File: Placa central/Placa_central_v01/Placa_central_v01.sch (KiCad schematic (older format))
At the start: 34 parts, among them J1 Conn_8.4V_PlacaAlimentação, J16 Conn_01x01_Motor1PonteHPCB, J2 Conn_01x02_ArduinoTxRx, J26 Conn_02x08_Odd_Even, J27 Conn_01x01_Motor2PonteHPCB, J28 Conn_01x01_Motor1PCBMotor, J29 Conn_01x01_Motor2PCBMotor, J3 Conn_01x01_ArduinoReset, J37 Conn_01x01_8.4VPonteH, J38 Conn_01x01_5VPonteH, J39 Conn_01x01_GNDPonteH, J4 Conn_GND_PlacaAlimentação, J40 Conn_01x01_Motor1PWM, J41 Conn_01x01_Motor1Dir1, J42 Conn_01x01_Motor1Dir2, J43 Conn_01x01_Motor2Dir1, J44 Conn_01x01_Motor2Dir2, J45 Conn_01x01_Motor2PWM, J48 Conn_01x01_5VEncoderEsq, J49 Conn_01x01_OutputEncoderEsq, J50 Conn_01x01_GNDEncoderEsq, J51 Conn_01x01_5VEncoderDir, J52 Conn_01x01_OutputEncoderDir, J53 Conn_01x01_GNDEncoderDir, SW3 SW_comando1

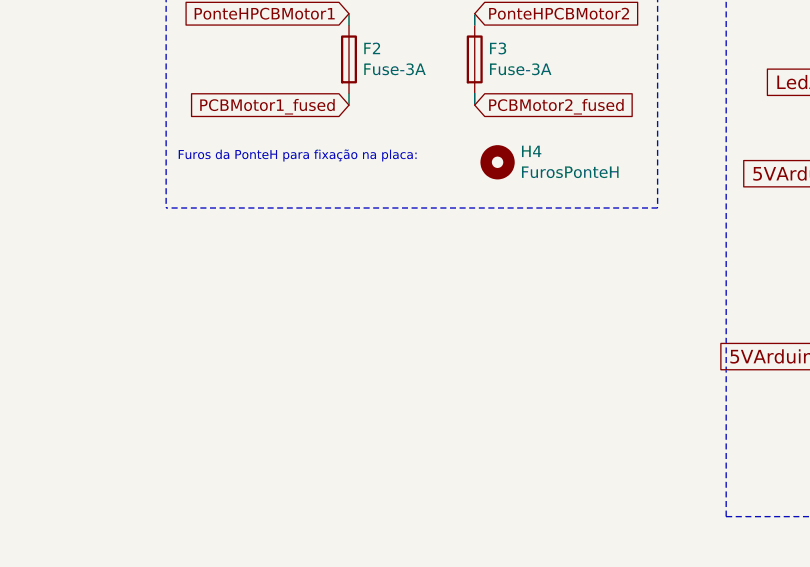
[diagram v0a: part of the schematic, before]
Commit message: Adicionada a zona de malha de ground, furos pendentes.
A zona de ground ainda não foi preenchida pois os furos da placa para fixação no acrílico requerem atualização.
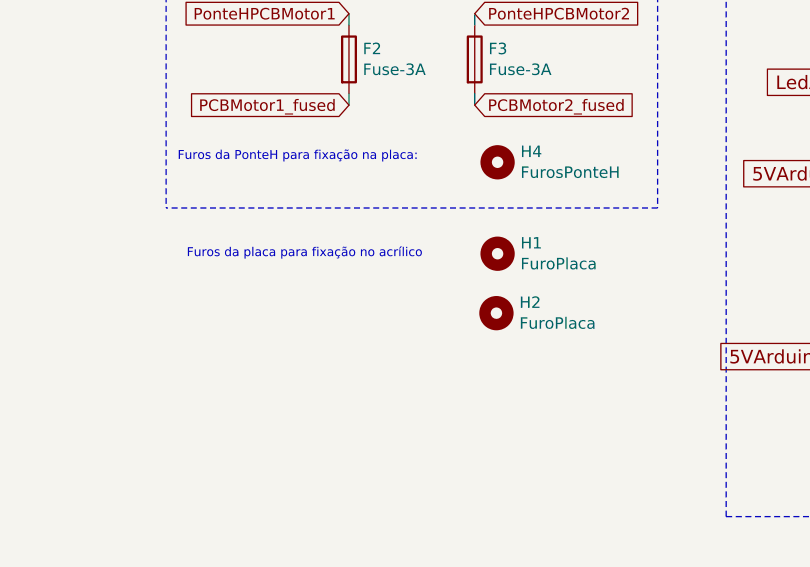
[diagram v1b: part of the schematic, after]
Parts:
- added H1, H2: FuroPlaca, Connector_Wire:SolderWirePad_1x01_Drill1mm, symbol Mechanical:MountingHole
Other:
- note added: "Furos da placa para fixação no acrílico"
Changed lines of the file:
@@
 Text GLabel 1650 2950 0    50   Input ~ 0
 ArduinoD13
+$Comp
+L Mechanical:MountingHole H1
+U 1 1 5D4C0D66
+P 7700 4050
+F 0 "H1" H 7800 4096 50  0000 L CNN
+F 1 "FuroPlaca" H 7800 4005 50  0000 L CNN
+F 2 "Connector_Wire:SolderWirePad_1x01_Drill1mm" H 7700 4050 50  0001 C CNN
+F 3 "~" H 7700 4050 50  0001 C CNN
+	1    7700 4050
+	1    0    0    -1
+$EndComp
+Text Notes 6340 4075 0    39   ~ 0
+Furos da placa para fixação no acrílico
+$Comp
+L Mechanical:MountingHole H2
+U 1 1 5D4C717E
+P 7695 4310
+F 0 "H2" H 7795 4356 50  0000 L CNN
+F 1 "FuroPlaca" H 7795 4265 50  0000 L CNN
+F 2 "Connector_Wire:SolderWirePad_1x01_Drill1mm" H 7695 4310 50  0001 C CNN
+F 3 "~" H 7695 4310 50  0001 C CNN
+	1    7695 4310
+	1    0    0    -1
+$EndComp
 $EndSCHEMATC

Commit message: Tamanho dos pinos corrigidos
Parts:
- H1, H2: footprint Connector_Wire:SolderWirePad_1x01_Drill1mm -> Connector_Wire:SolderWirePad_1x01_Drill2.5mm
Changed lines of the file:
@@
 F 0 "H1" H 7800 4096 50  0000 L CNN
 F 1 "FuroPlaca" H 7800 4005 50  0000 L CNN
-F 2 "Connector_Wire:SolderWirePad_1x01_Drill1mm" H 7700 4050 50  0001 C CNN
+F 2 "Connector_Wire:SolderWirePad_1x01_Drill2.5mm" H 7700 4050 50  0001 C CNN
 F 3 "~" H 7700 4050 50  0001 C CNN
 	1    7700 4050
@@
 F 0 "H2" H 7795 4356 50  0000 L CNN
 F 1 "FuroPlaca" H 7795 4265 50  0000 L CNN
-F 2 "Connector_Wire:SolderWirePad_1x01_Drill1mm" H 7695 4310 50  0001 C CNN
+F 2 "Connector_Wire:SolderWirePad_1x01_Drill2.5mm" H 7695 4310 50  0001 C CNN
 F 3 "~" H 7695 4310 50  0001 C CNN
 	1    7695 4310

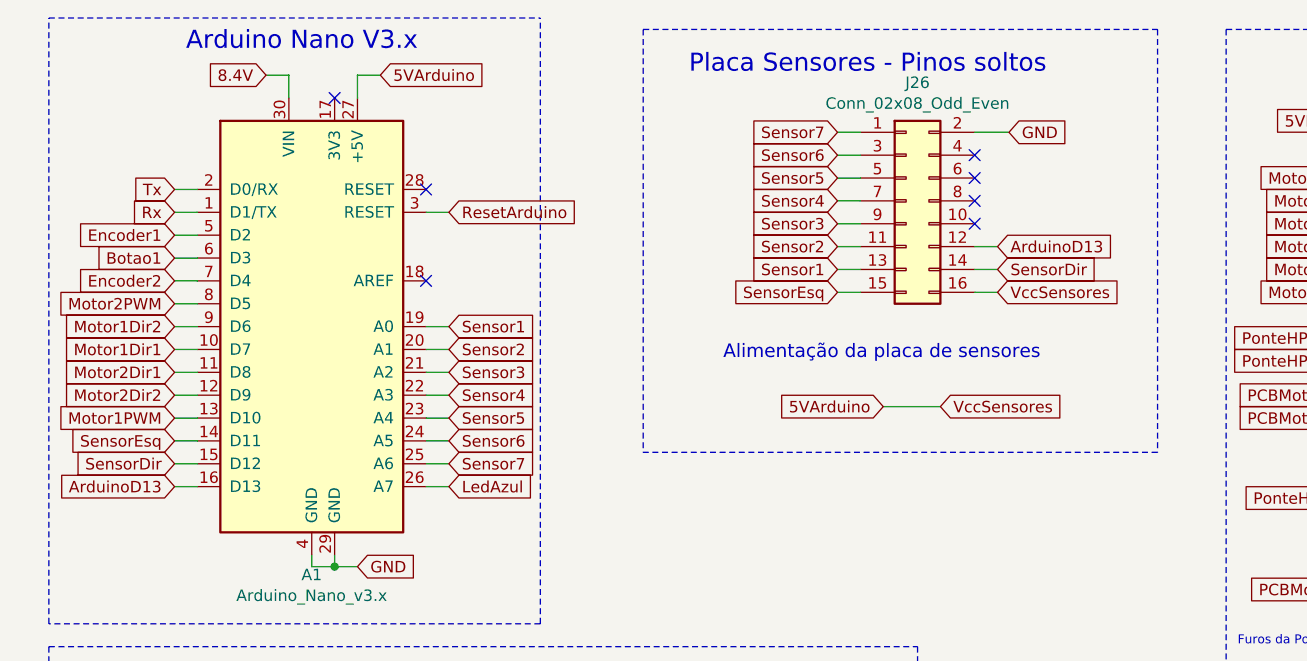
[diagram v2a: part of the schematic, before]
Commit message: Pinos do conector alterados, conector agora está exclusivamente conectado na malha verde.
Criado net do Sensor8, quando houver a necessidade de utilizar a placa vermelha.
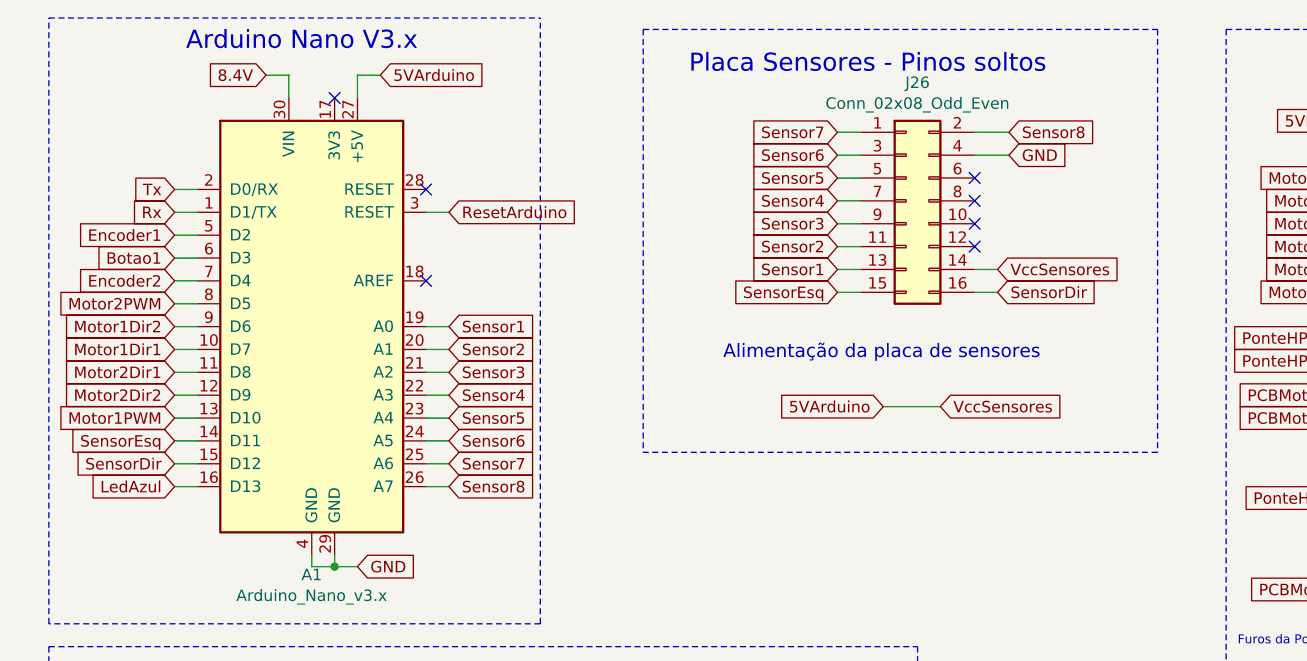
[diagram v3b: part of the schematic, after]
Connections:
- net 5VArduino: now also J26.14 (Pin_14); no longer J26.16 (Pin_16)
- net GND: now also J26.4 (Pin_4); no longer J26.2 (Pin_2)
- net LedAzul: now also A1.16 (D13); no longer A1.26 (A7)
- net SensorDir: now also J26.16 (Pin_16); no longer J26.14 (Pin_14)
- net ArduinoD13: no longer names the net of J26.12 (Pin_12)
- net ArduinoD13: no longer A1.16 (D13)
- new net Sensor8: A1.26 (A7), J26.2 (Pin_2)
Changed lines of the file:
@@
 Text GLabel 4550 2100 0    50   Input ~ 0
 SensorEsq
-Text GLabel 5250 2000 2    50   Input ~ 0
+Text GLabel 5250 2100 2    50   Input ~ 0
 SensorDir
 Text Notes 4050 2400 0    59   ~ 0
@@
 Text GLabel 2850 2850 2    50   Input ~ 0
 Sensor7
-Text GLabel 2850 2950 2    50   Input ~ 0
+Text GLabel 1650 2950 0    50   Input ~ 0
 LedAzul
 Text GLabel 1650 1650 0    50   Input ~ 0
@@
 ResetArduino
 NoConn ~ 2750 1650
-Text GLabel 5300 1400 2    50   Input ~ 0
+Text GLabel 5300 1500 2    50   Input ~ 0
 GND
 Text GLabel 5000 2600 2    50   Input ~ 0
 VccSensores
-Text GLabel 5250 2100 2    50   Input ~ 0
+Text GLabel 5250 2000 2    50   Input ~ 0
 VccSensores
 Text GLabel 4750 2600 0    50   Input ~ 0
@@
 NoConn ~ 5150 1600
 NoConn ~ 5150 1700
-NoConn ~ 5150 1500
 Wire Wire Line
 	2150 1150 2150 1250
@@
 Wire Wire Line
 	1750 2250 1650 2250
-Text GLabel 5250 1900 2    50   Input ~ 0
-ArduinoD13
 Wire Wire Line
 	5150 2000 5250 2000
@@
 	1    0    0    -1
 $EndComp
-Wire Wire Line
-	5250 1900 5150 1900
 NoConn ~ 5150 1800
 Wire Wire Line
 	5150 1400 5300 1400
-Text GLabel 1650 2950 0    50   Input ~ 0
-ArduinoD13
 $Comp
 L Mechanical:MountingHole H1
@@
 	1    0    0    -1
 $EndComp
+Text GLabel 2850 2950 2    50   Input ~ 0
+Sensor8
+Text GLabel 5300 1400 2    50   Input ~ 0
+Sensor8
+Wire Wire Line
+	5300 1500 5150 1500
+NoConn ~ 5150 1900
 $EndSCHEMATC

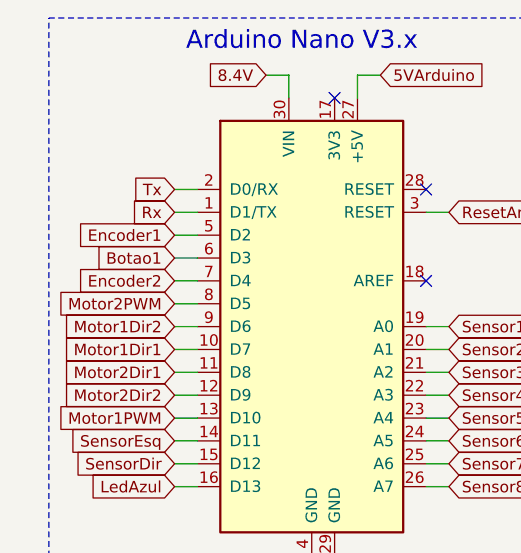
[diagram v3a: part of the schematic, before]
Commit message: Mudancas criticas na PCB Central, ainda ha pendencias
Foi trocado o pino do botao pelo pino do encoder. Os encoders devem estar obrigatoriamente nos pinos D2 e D3:
Encoder2 para o pino 6 (D3)
Botao1 para o pino 7 (D4);
Aumentadas as dimensoes dos pads conectores do arduino, para mais seguranca ao furar;
Pads do conector modificados para melhor seguranca ao furar;
Clearance da malha de ground aumentada de 0.5 para 0.7
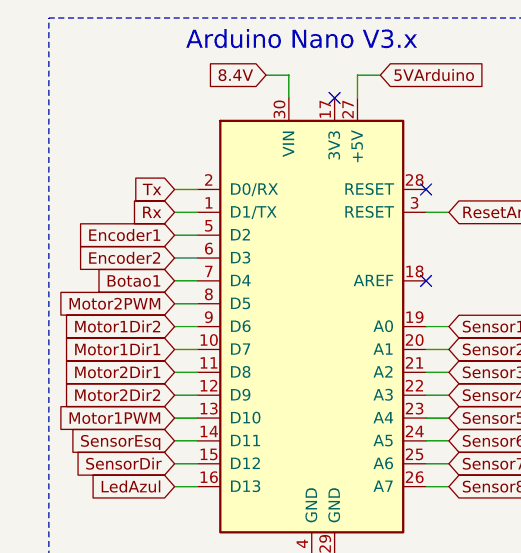
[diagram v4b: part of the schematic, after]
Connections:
- net Botao1: now also A1.7 (D4); no longer A1.6 (D3)
- net Encoder2: now also A1.6 (D3); no longer A1.7 (D4)
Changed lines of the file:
@@
 EESchema Schematic File Version 4
 LIBS:Placa_central_v01-cache
-EELAYER 30 0
+EELAYER 26 0
 EELAYER END
 $Descr A4 11693 8268
@@
 Text GLabel 1650 1850 0    50   Input ~ 0
 Encoder1
-Text GLabel 1650 2050 0    50   Input ~ 0
+Text GLabel 1650 1950 0    50   Input ~ 0
 Encoder2
 $Comp
@@
 Text GLabel 1650 2550 0    50   Input ~ 0
 Motor2Dir2
-Text GLabel 1650 1950 0    50   Input ~ 0
+Text GLabel 1650 2050 0    50   Input ~ 0
 Botao1
 Text GLabel 2550 1150 2    50   Input ~ 0

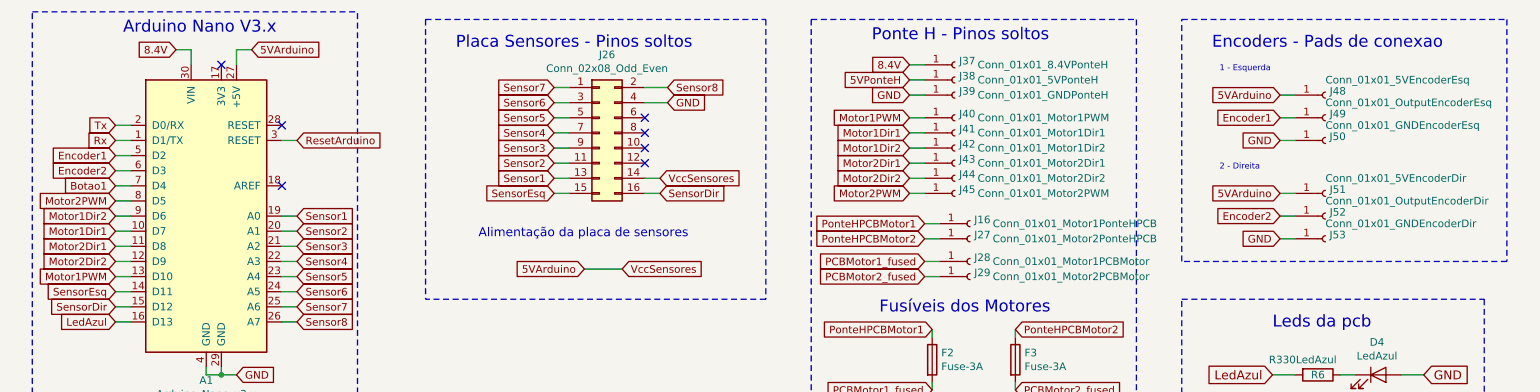
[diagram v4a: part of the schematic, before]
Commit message: Acertada as placas e os pdfs
Acertada as placas centrais, de alimentação e de conector.
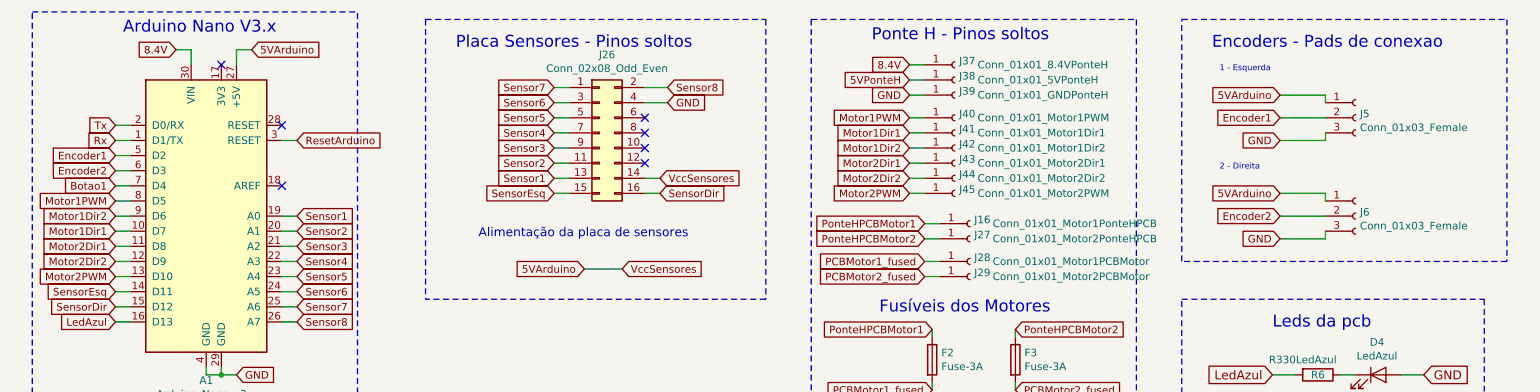
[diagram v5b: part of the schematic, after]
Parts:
- removed J48: Conn_01x01_5VEncoderEsq, Connector_Wire:SolderWirePad_1x01_Drill0.8mm, symbol Connector:Conn_01x01_Female
- removed J49: Conn_01x01_OutputEncoderEsq, Connector_PinSocket_2.54mm:PinSocket_1x01_P2.54mm_Vertical, symbol Connector:Conn_01x01_Female
- removed J50: Conn_01x01_GNDEncoderEsq, Connector_Wire:SolderWirePad_1x01_Drill0.8mm, symbol Connector:Conn_01x01_Female
- removed J51: Conn_01x01_5VEncoderDir, Connector_Wire:SolderWirePad_1x01_Drill0.8mm, symbol Connector:Conn_01x01_Female
- removed J52: Conn_01x01_OutputEncoderDir, Connector_PinSocket_2.54mm:PinSocket_1x01_P2.54mm_Vertical, symbol Connector:Conn_01x01_Female
- removed J53: Conn_01x01_GNDEncoderDir, Connector_Wire:SolderWirePad_1x01_Drill0.8mm, symbol Connector:Conn_01x01_Female
- added J5, J6: Conn_01x03_Female, Connector_Molex:Molex_KK-254_AE-6410-03A_1x03_P2.54mm_Vertical, symbol Connector:Conn_01x03_Female
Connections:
- net 5VArduino: now also J5.1 (Pin_1), J6.1 (Pin_1)
- net Encoder1: now also J5.2 (Pin_2)
- net Encoder2: now also J6.2 (Pin_2)
- net GND: now also J5.3 (Pin_3), J6.3 (Pin_3)
- net Motor1PWM: now also A1.8 (D5); no longer A1.13 (D10)
- net Motor2PWM: now also A1.13 (D10); no longer A1.8 (D5)
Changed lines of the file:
@@
 EESchema Schematic File Version 4
 LIBS:Placa_central_v01-cache
-EELAYER 26 0
+EELAYER 29 0
 EELAYER END
 $Descr A4 11693 8268
@@
 Text GLabel 1650 2750 0    50   Input ~ 0
 SensorEsq
-Text GLabel 1650 2650 0    50   Input ~ 0
-Motor1PWM
-Text GLabel 1650 2150 0    50   Input ~ 0
-Motor2PWM
 Text GLabel 1650 2350 0    50   Input ~ 0
 Motor1Dir1
@@
 Text Notes 9250 4100 0    79   ~ 0
 Botoes da pcb
-$Comp
-L Connector:Conn_01x01_Female J48
-U 1 1 5D18DC68
-P 9650 1450
-F 0 "J48" H 9678 1476 50  0000 L CNN
-F 1 "Conn_01x01_5VEncoderEsq" H 9650 1550 50  0000 L CNN
-F 2 "Connector_Wire:SolderWirePad_1x01_Drill0.8mm" H 9650 1450 50  0001 C CNN
-F 3 "~" H 9650 1450 50  0001 C CNN
-	1    9650 1450
-	1    0    0    -1
-$EndComp
-$Comp
-L Connector:Conn_01x01_Female J49
-U 1 1 5D18E3FC
-P 9650 1600
-F 0 "J49" H 9678 1626 50  0000 L CNN
-F 1 "Conn_01x01_OutputEncoderEsq" H 9650 1700 50  0000 L CNN
-F 2 "Connector_PinSocket_2.54mm:PinSocket_1x01_P2.54mm_Vertical" H 9650 1600 50  0001 C CNN
-F 3 "~" H 9650 1600 50  0001 C CNN
-	1    9650 1600
-	1    0    0    -1
-$EndComp
-$Comp
-L Connector:Conn_01x01_Female J50
-U 1 1 5D18E464
-P 9650 1750
-F 0 "J50" H 9677 1776 50  0000 L CNN
-F 1 "Conn_01x01_GNDEncoderEsq" H 9650 1850 50  0000 L CNN
-F 2 "Connector_Wire:SolderWirePad_1x01_Drill0.8mm" H 9650 1750 50  0001 C CNN
-F 3 "~" H 9650 1750 50  0001 C CNN
-	1    9650 1750
-	1    0    0    -1
-$EndComp
 Text GLabel 9350 1600 0    50   Input ~ 0
 Encoder1
@@
 Text GLabel 9350 1750 0    50   Input ~ 0
 GND
-$Comp
-L Connector:Conn_01x01_Female J51
-U 1 1 5D19974C
-P 9650 2100
-F 0 "J51" H 9678 2126 50  0000 L CNN
-F 1 "Conn_01x01_5VEncoderDir" H 9650 2200 50  0000 L CNN
-F 2 "Connector_Wire:SolderWirePad_1x01_Drill0.8mm" H 9650 2100 50  0001 C CNN
-F 3 "~" H 9650 2100 50  0001 C CNN
-	1    9650 2100
-	1    0    0    -1
-$EndComp
-$Comp
-L Connector:Conn_01x01_Female J52
-U 1 1 5D199753
-P 9650 2250
-F 0 "J52" H 9678 2276 50  0000 L CNN
-F 1 "Conn_01x01_OutputEncoderDir" H 9650 2350 50  0000 L CNN
-F 2 "Connector_PinSocket_2.54mm:PinSocket_1x01_P2.54mm_Vertical" H 9650 2250 50  0001 C CNN
-F 3 "~" H 9650 2250 50  0001 C CNN
-	1    9650 2250
-	1    0    0    -1
-$EndComp
-$Comp
-L Connector:Conn_01x01_Female J53
-U 1 1 5D19975A
-P 9650 2400
-F 0 "J53" H 9677 2426 50  0000 L CNN
-F 1 "Conn_01x01_GNDEncoderDir" H 9650 2500 50  0000 L CNN
-F 2 "Connector_Wire:SolderWirePad_1x01_Drill0.8mm" H 9650 2400 50  0001 C CNN
-F 3 "~" H 9650 2400 50  0001 C CNN
-	1    9650 2400
-	1    0    0    -1
-$EndComp
 Text GLabel 9350 2250 0    50   Input ~ 0
 Encoder2
@@
 Wire Notes Line
 	1100 900  3250 900
-Wire Wire Line
-	9350 1450 9450 1450
-Wire Wire Line
-	9350 1600 9450 1600
-Wire Wire Line
-	9350 1750 9450 1750
-Wire Wire Line
-	9350 2100 9450 2100
-Wire Wire Line
-	9350 2250 9450 2250
-Wire Wire Line
-	9350 2400 9450 2400
 Wire Notes Line
 	8700 950  10850 950
@@
 	5300 1500 5150 1500
 NoConn ~ 5150 1900
+Wire Wire Line
+	9650 1450 9650 1500
+Wire Wire Line
+	9350 1450 9650 1450
+Wire Wire Line
+	9350 1600 9650 1600
+Wire Wire Line
+	9650 1750 9650 1700
+Wire Wire Line
+	9350 1750 9650 1750
+Wire Wire Line
+	9650 2100 9650 2150
+Wire Wire Line
+	9350 2100 9650 2100
+Wire Wire Line
+	9350 2250 9650 2250
+Wire Wire Line
+	9650 2400 9650 2350
+Wire Wire Line
+	9350 2400 9650 2400
+$Comp
+L Connector:Conn_01x03_Female J5
+U 1 1 5D730FE8
+P 9850 1600
+F 0 "J5" H 9878 1626 50  0000 L CNN
+F 1 "Conn_01x03_Female" H 9878 1535 50  0000 L CNN
+F 2 "Connector_Molex:Molex_KK-254_AE-6410-03A_1x03_P2.54mm_Vertical" H 9850 1600 50  0001 C CNN
+F 3 "~" H 9850 1600 50  0001 C CNN
+	1    9850 1600
+	1    0    0    -1
+$EndComp
+$Comp
+L Connector:Conn_01x03_Female J6
+U 1 1 5D731C8E
+P 9850 2250
+F 0 "J6" H 9878 2276 50  0000 L CNN
+F 1 "Conn_01x03_Female" H 9878 2185 50  0000 L CNN
+F 2 "Connector_Molex:Molex_KK-254_AE-6410-03A_1x03_P2.54mm_Vertical" H 9850 2250 50  0001 C CNN
+F 3 "~" H 9850 2250 50  0001 C CNN
+	1    9850 2250
+	1    0    0    -1
+$EndComp
+Text GLabel 1650 2150 0    50   Input ~ 0
+Motor1PWM
+Text GLabel 1650 2650 0    50   Input ~ 0
+Motor2PWM
 $EndSCHEMATC
